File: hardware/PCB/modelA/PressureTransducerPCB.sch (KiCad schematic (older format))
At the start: 10 parts

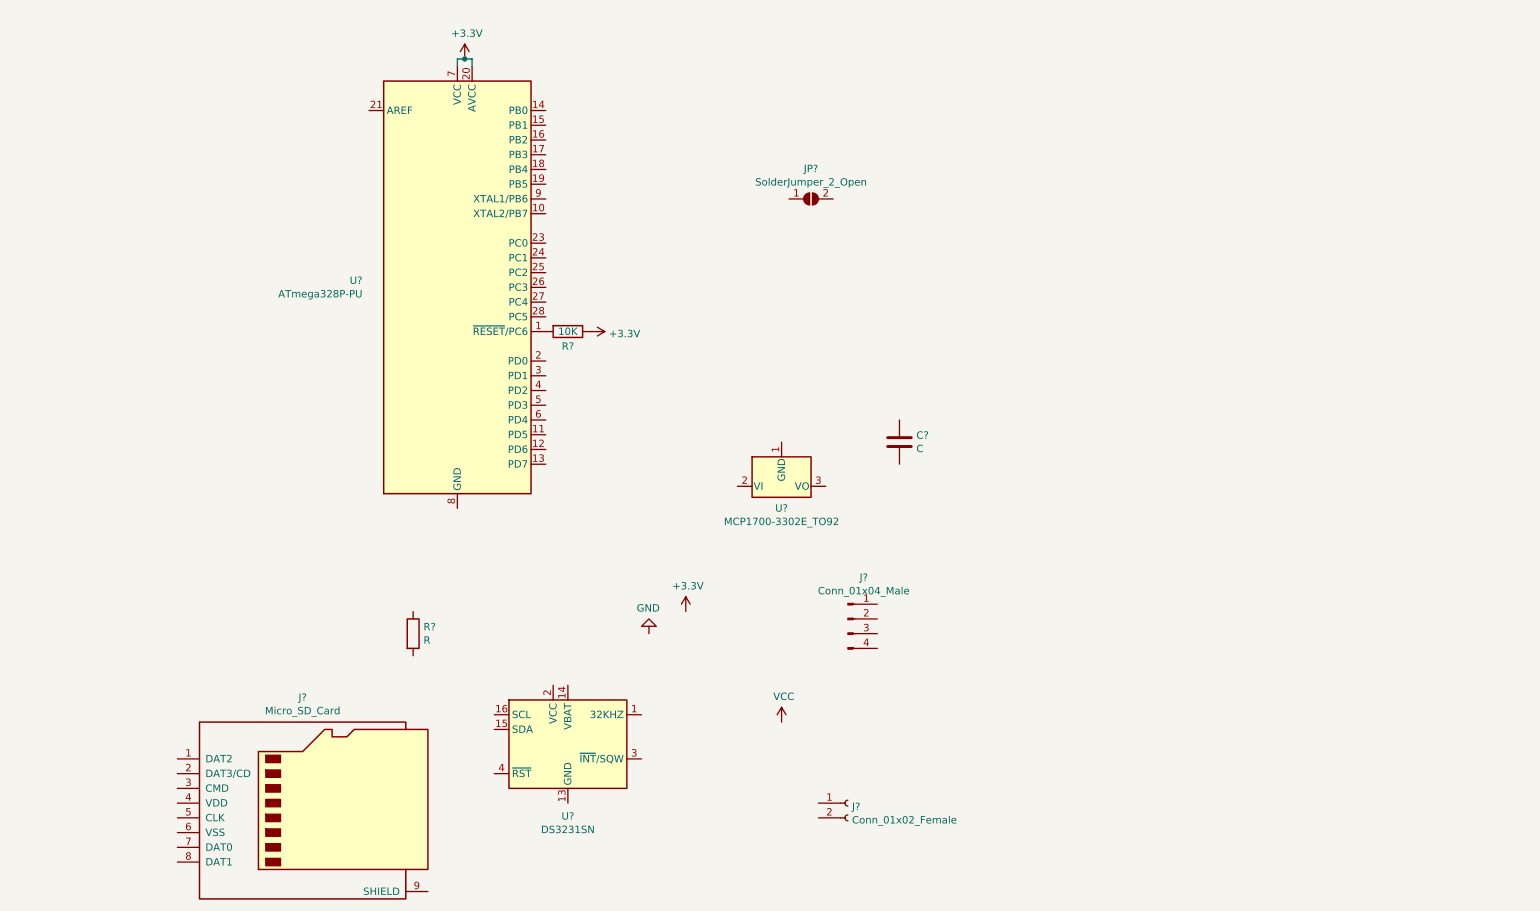
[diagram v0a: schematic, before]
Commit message: Finish first version of schematic
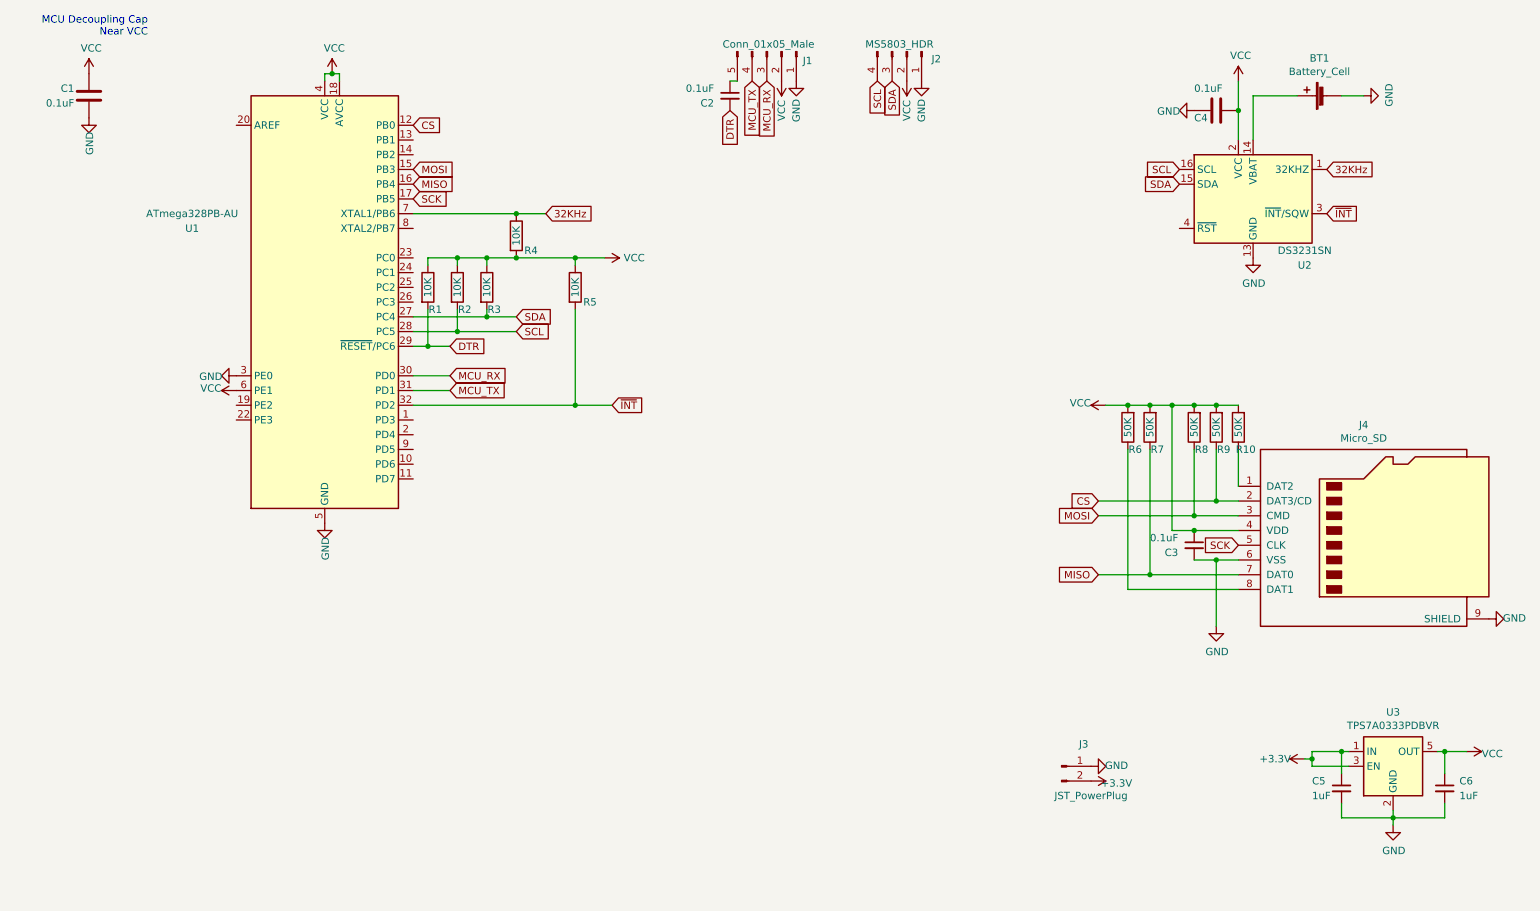
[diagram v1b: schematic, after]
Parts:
- removed C?: C, symbol Device:C
- removed J?: Conn_01x02_Female, symbol Connector:Conn_01x02_Female
- removed JP?: SolderJumper_2_Open, symbol Jumper:SolderJumper_2_Open
- removed R?: R, symbol Device:R
- removed U?: ATmega328P-PU, Package_DIP:DIP-28_W7.62mm, symbol MCU_Microchip_ATmega:ATmega328P-PU
- removed U?: MCP1700-3302E_TO92, Package_TO_SOT_THT:TO-92_Inline, symbol Regulator_Linear:MCP1700-3302E_TO92
- added BT1: Battery_Cell, Battery:BatteryHolder_Keystone_3002_1x2032, symbol Device:Battery_Cell
- added C1, C4: 0.1uF, Capacitor_SMD:C_0805_2012Metric, symbol Device:C
- added C2, C3: 0.1uF, Capacitor_SMD:C_0805_2012Metric, symbol Device:C_Small
- added C5, C6: 1uF, Capacitor_SMD:C_0402_1005Metric, symbol Device:C_Small
- added J1: Conn_01x05_Male, Connector_PinHeader_2.54mm:PinHeader_1x05_P2.54mm_Vertical, symbol Connector:Conn_01x05_Male
- added J3: JST_PowerPlug, Connector_JST:JST_PH_S2B-PH-K_1x02_P2.00mm_Horizontal, symbol Connector:Conn_01x02_Male
- added R10, R6, R7, R8, R9: 50K, Resistor_SMD:R_1206_3216Metric, symbol Device:R
- added R2, R3, R4, R5: 10K, Resistor_SMD:R_0805_2012Metric, symbol Device:R
- added U1: ATmega328PB-AU, Package_QFP:TQFP-32_7x7mm_P0.8mm, symbol MCU_Microchip_ATmega:ATmega328PB-AU
- added U3: TPS7A0333PDBVR, Package_TO_SOT_SMD:SOT-23-5, symbol Regulator_Linear:TPS7A0530PDBV
- J2: renamed from J?; value Conn_01x04_Male -> MS5803_HDR; footprint (none) -> Connector_JST:JST_PH_S5B-PH-K_1x05_P2.00mm_Horizontal
- J4: renamed from J?; value Micro_SD_Card -> Micro_SD; footprint (none) -> Connector_Card:microSD_HC_Hirose_DM3D-SF
- R1: renamed from R?; footprint (none) -> Resistor_SMD:R_0805_2012Metric
- gave numbers to parts that had none: 1
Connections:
- net +3V3: now also C5.1, J3.2 (Pin_2), U3.1 (IN), U3.3 (EN); no longer R1.1
- net GND: now also J2.1 (Pin_1), J4.6 (VSS), J4.9 (SHIELD), U2.10 (GND), U2.11 (GND), U2.12 (GND), U2.13 (GND), U2.5 (GND), U2.6 (GND), U2.7 (GND), U2.8 (GND), U2.9 (GND), BT1.2 (-), C1.1, C3.2, C4.2, C5.2, C6.2, J1.1 (Pin_1), J3.1 (Pin_1), U1.21 (GND), U1.3 (PE0), U1.5 (GND), U3.2 (GND)
- net VCC: now also J2.2 (Pin_2), J4.4 (VDD), R1.1, U2.2 (VCC), C1.2, C3.1, C4.1, C6.1, J1.2 (Pin_2), R10.2, R2.1, R3.1, R4.2, R5.1, R6.2, R7.2, R8.2, R9.2, U1.18 (AVCC), U1.4 (VCC), U1.6 (PE1), U3.5 (OUT)
- net DTR: now reaches R1.2
- net DTR: now also C2.2, U1.29 (~RESET~/PC6)
- net SDA: now reaches J2.3 (Pin_3)
- net SDA: now also U2.15 (SDA), R3.2, U1.27 (PC4)
- net SCL: now reaches J2.4 (Pin_4)
- net SCL: now also U2.16 (SCL), R2.2, U1.28 (PC5)
- net 32KHz: now reaches U2.1 (32KHZ)
- net 32KHz: now also R4.1, U1.7 (XTAL1/PB6)
- net at U2.14 (VBAT): now also BT1.1 (+)
- net ~INT: now reaches U2.3 (~INT~/SQW)
- net ~INT: now also R5.2, U1.32 (PD2)
- net at J4.1 (DAT2): now also R10.1
- net CS: now reaches J4.2 (DAT3/CD)
- net CS: now also R9.1, U1.12 (PB0)
- net MOSI: now reaches J4.3 (CMD)
- net MOSI: now also R8.1, U1.15 (PB3)
- net SCK: now reaches J4.5 (CLK)
- net SCK: now also U1.17 (PB5)
- net MISO: now reaches J4.7 (DAT0)
- net MISO: now also R7.1, U1.16 (PB4)
- net at J4.8 (DAT1): now also R6.1
- new net: C2.1, J1.5 (Pin_5)
- new net MCU_RX: J1.3 (Pin_3), U1.30 (PD0)
- new net MCU_TX: J1.4 (Pin_4), U1.31 (PD1)
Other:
- note added: "MCU Decoupling Cap\nNear VCC"
- moved on the sheet: J2, J4, R1, U2

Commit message: Old PCB changes
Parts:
- removed R5: 10K, Resistor_SMD:R_0805_2012Metric, symbol Device:R
- C1, C2, C3, C4: footprint Capacitor_SMD:C_0805_2012Metric -> Capacitor_SMD:C_0402_1005Metric
- J2: footprint Connector_JST:JST_PH_S5B-PH-K_1x05_P2.00mm_Horizontal -> Connector_JST:JST_PH_S4B-PH-K_1x04_P2.00mm_Horizontal
- J4: footprint Connector_Card:microSD_HC_Hirose_DM3D-SF -> Connector_Card:microSD_HC_Hirose_DM3BT-DSF-PEJS
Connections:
- net +3V3 renamed +3V8
- net DTR renamed ~RESET
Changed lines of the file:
@@
 $EndDescr
-$Comp
-L power:+3.3V #PWR019
-U 1 1 609C0B30
-P 9250 5600
-F 0 "#PWR019" H 9250 5450 50  0001 C CNN
-F 1 "+3.3V" V 9250 5800 50  0000 C CNN
-F 2 "" H 9250 5600 50  0001 C CNN
-F 3 "" H 9250 5600 50  0001 C CNN
-	1    9250 5600
-	0    -1   -1   0
-$EndComp
 $Comp
 L Device:R R1
@@
 F 0 "J4" H 9650 4767 50  0000 C CNN
 F 1 "Micro_SD" H 9650 4676 50  0000 C CNN
-F 2 "Connector_Card:microSD_HC_Hirose_DM3D-SF" H 10850 4350 50  0001 C CNN
+F 2 "Connector_Card:microSD_HC_Hirose_DM3BT-DSF-PEJS" H 10850 4350 50  0001 C CNN
 F 3 "http://katalog.we-online.de/em/datasheet/693072010801.pdf" H 9700 4050 50  0001 C CNN
 	1    9700 4050
@@
 $EndComp
 $Comp
-L power:+3.3V #PWR013
-U 1 1 60ACC880
-P 7800 5750
-F 0 "#PWR013" H 7800 5600 50  0001 C CNN
-F 1 "+3.3V" V 7815 5923 50  0000 C CNN
-F 2 "" H 7800 5750 50  0001 C CNN
-F 3 "" H 7800 5750 50  0001 C CNN
-	1    7800 5750
-	0    1    1    0
-$EndComp
-$Comp
 L power:GND #PWR012
 U 1 1 60ACE656
@@
 F 0 "C4" V 8700 1050 50  0000 L CNN
 F 1 "0.1uF" V 8500 1050 50  0000 L CNN
-F 2 "Capacitor_SMD:C_0805_2012Metric" H 8688 1050 50  0001 C CNN
+F 2 "Capacitor_SMD:C_0402_1005Metric" H 8688 1050 50  0001 C CNN
 F 3 "~" H 8650 1200 50  0001 C CNN
 	1    8650 1200
@@
 F 0 "C1" H 1100 1050 50  0000 L CNN
 F 1 "0.1uF" H 1100 1150 50  0000 L CNN
-F 2 "Capacitor_SMD:C_0805_2012Metric" H 1038 950 50  0001 C CNN
+F 2 "Capacitor_SMD:C_0402_1005Metric" H 1038 950 50  0001 C CNN
 F 3 "~" H 1000 1100 50  0001 C CNN
 	1    1000 1100
@@
 Text GLabel 9400 1900 2    50   Input ~ 0
 ~INT
-Text GLabel 4550 3200 2    50   Input ~ 0
+Text GLabel 3300 3200 2    50   Input ~ 0
 ~INT
 Connection ~ 3900 1900
@@
 F 0 "C3" H 8300 4100 50  0000 L CNN
 F 1 "0.1uF" H 8200 4200 50  0000 L CNN
-F 2 "Capacitor_SMD:C_0805_2012Metric" H 8500 4150 50  0001 C CNN
+F 2 "Capacitor_SMD:C_0402_1005Metric" H 8500 4150 50  0001 C CNN
 F 3 "~" H 8500 4150 50  0001 C CNN
 	1    8500 4150
@@
 F 0 "J2" V 6600 1000 50  0000 C CNN
 F 1 "MS5803_HDR" V 6500 750 50  0000 C CNN
-F 2 "Connector_JST:JST_PH_S5B-PH-K_1x05_P2.00mm_Horizontal" H 6550 800 50  0001 C CNN
+F 2 "Connector_JST:JST_PH_S4B-PH-K_1x04_P2.00mm_Horizontal" H 6550 800 50  0001 C CNN
 F 3 "~" H 6550 800 50  0001 C CNN
 	1    6550 800
@@
 	1    0    0    -1
 $EndComp
-Wire Wire Line
-	4300 3200 4550 3200
-Connection ~ 4300 3200
-Wire Wire Line
-	4300 2200 4500 2200
-Connection ~ 4300 2200
-Wire Wire Line
-	3200 3200 4300 3200
-Wire Wire Line
-	3900 2200 4300 2200
-Wire Wire Line
-	4300 2250 4300 2200
-Wire Wire Line
-	4300 2550 4300 3200
-$Comp
-L Device:R R5
-U 1 1 60B25EED
-P 4300 2400
-F 0 "R5" H 4400 2300 50  0000 C CNN
-F 1 "10K" V 4300 2400 50  0000 C CNN
-F 2 "Resistor_SMD:R_0805_2012Metric" V 4230 2400 50  0001 C CNN
-F 3 "~" H 4300 2400 50  0001 C CNN
-	1    4300 2400
-	1    0    0    -1
-$EndComp
 $Comp
 L Connector:Conn_01x05_Male J1
@@
 Text GLabel 5500 1000 3    50   Input ~ 0
 MCU_TX
-Text GLabel 5350 1200 3    50   Input ~ 0
-DTR
 $Comp
 L Device:C_Small C2
@@
 F 0 "C2" H 5150 1050 50  0000 L CNN
 F 1 "0.1uF" H 5050 1150 50  0000 L CNN
-F 2 "Capacitor_SMD:C_0805_2012Metric" H 5350 1100 50  0001 C CNN
+F 2 "Capacitor_SMD:C_0402_1005Metric" H 5350 1100 50  0001 C CNN
 F 3 "~" H 5350 1100 50  0001 C CNN
 	1    5350 1100
@@
 	5350 1000 5400 1000
 Text GLabel 3450 2800 2    50   Input ~ 0
-DTR
+~RESET
 Wire Wire Line
 	3300 2800 3450 2800
@@
 Text GLabel 3200 1300 2    50   Input ~ 0
 CS
+$Comp
+L power:+3V8 #PWR0101
+U 1 1 60AC43B2
+P 7800 5750
+F 0 "#PWR0101" H 7800 5600 50  0001 C CNN
+F 1 "+3V8" V 7815 5878 50  0000 L CNN
+F 2 "" H 7800 5750 50  0001 C CNN
+F 3 "" H 7800 5750 50  0001 C CNN
+	1    7800 5750
+	0    1    1    0
+$EndComp
+$Comp
+L power:+3V8 #PWR0102
+U 1 1 60AC8134
+P 9250 5600
+F 0 "#PWR0102" H 9250 5450 50  0001 C CNN
+F 1 "+3V8" V 9265 5728 50  0000 L CNN
+F 2 "" H 9250 5600 50  0001 C CNN
+F 3 "" H 9250 5600 50  0001 C CNN
+	1    9250 5600
+	0    -1   -1   0
+$EndComp
+Wire Wire Line
+	3900 2200 4500 2200
+Wire Wire Line
+	3200 3200 3300 3200
+Text GLabel 5350 1200 3    50   Input ~ 0
+~RESET
 $EndSCHEMATC
